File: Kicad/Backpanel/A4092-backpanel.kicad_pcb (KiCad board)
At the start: 2 copper layers, 45 x 90.5 mm, 4 parts, among them J1 Conn_02x25_Odd_Even, J2 5787170-5

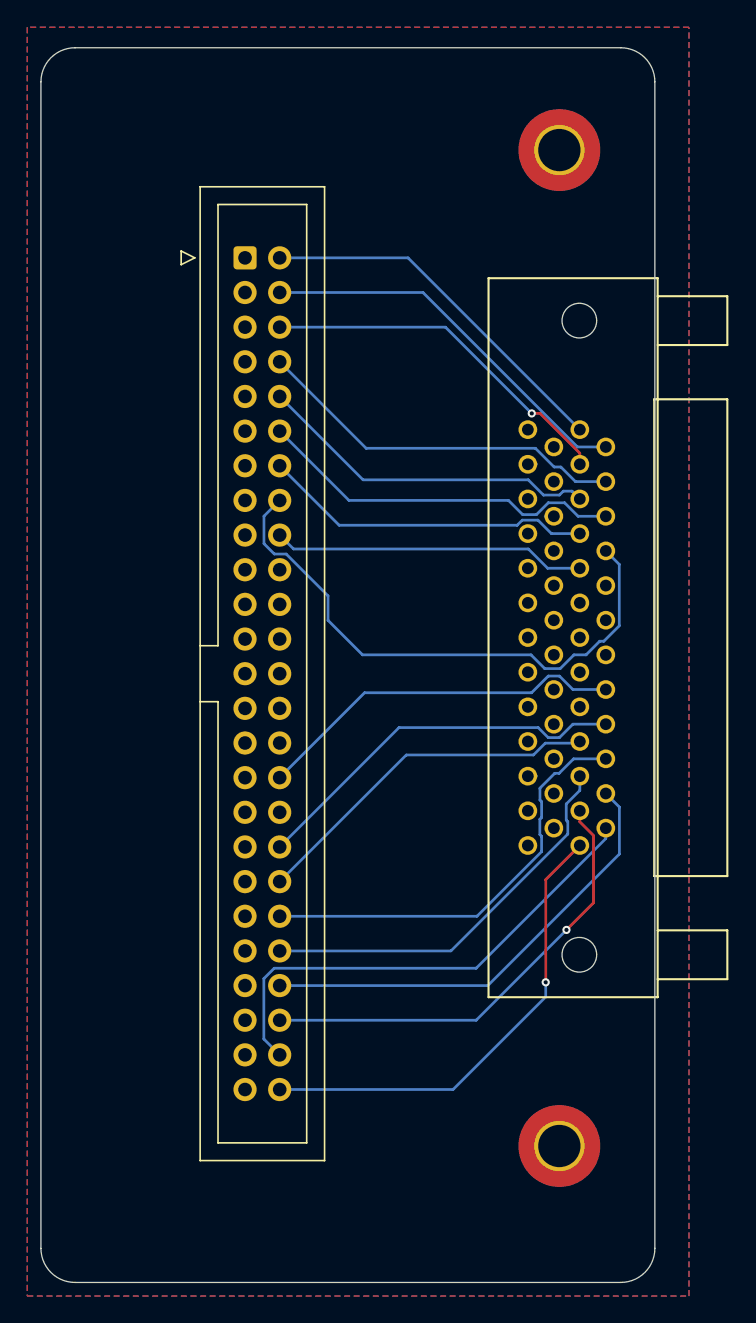
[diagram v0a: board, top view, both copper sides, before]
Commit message: Update Backpanel for smaller footprint
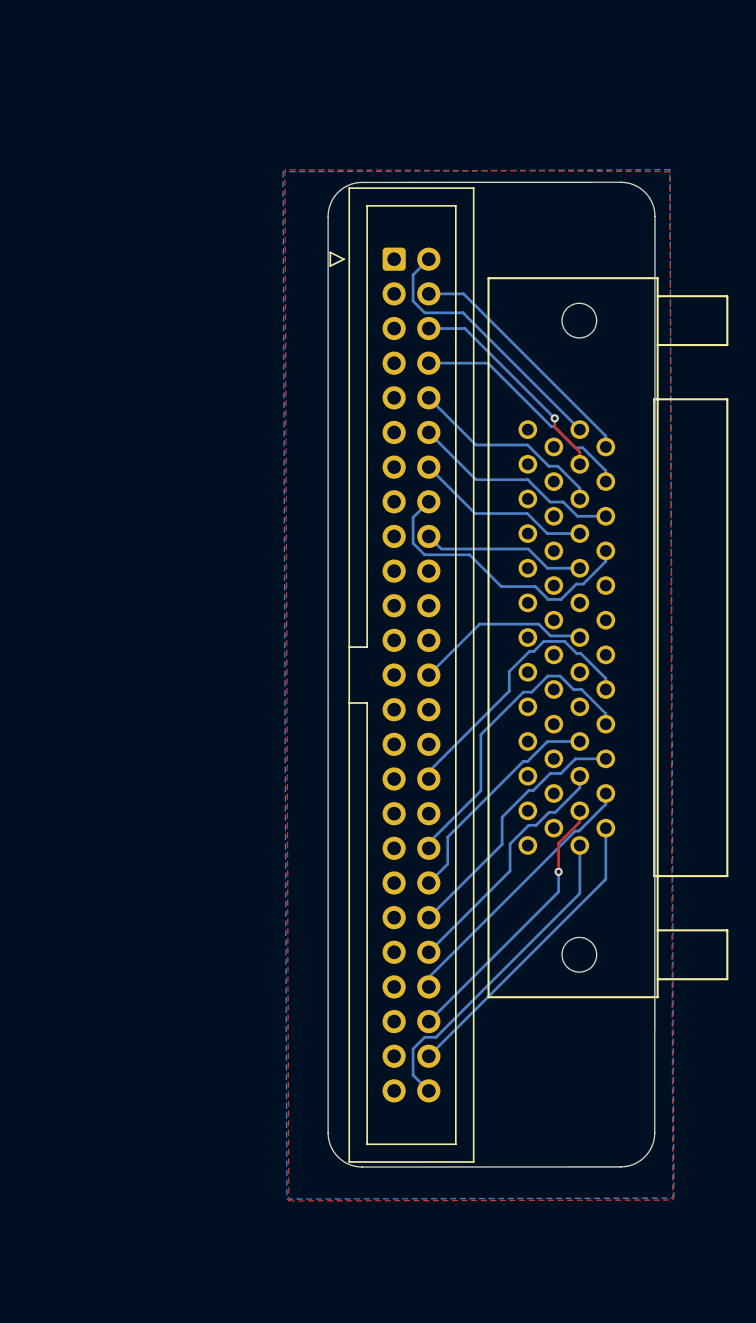
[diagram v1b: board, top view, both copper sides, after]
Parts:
- removed H1, H2: MOUNT_HOLE, StefanHamminga/SH_Mechanical.pretty:MOUNT_HOLE_M3
- moved J1 10.9 mm to (155.9, 65.5)
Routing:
- net SCDAT7: track 41.7 -> 21.3 mm
- net SCTRL_REQ: track 36.2 -> 22.1 mm
- net SCTRL_SEL: track 33.7 -> 19.7 mm
- net SCTRL_CD: track 33.7 -> 20.0 mm
- net SCSI_TERMPWR: track 0.00 -> 13.0 mm
- net SCTRL_RST: track 31.7 -> 19.0 mm
- net SCDAT5: track 27.2 -> 15.5 mm
- net SCTRL_MSG: track 29.4 -> 18.1 mm
- net SCDAT6: track 24.4 -> 13.1 mm
- net SCDATP: track 23.0 -> 12.0 mm
- net SCDAT4: track 25.3 -> 14.6 mm
- net SCDAT2: track 26.6 -> 16.1 mm
- net SCDAT3: track 27.5 -> 17.0 mm
- net SCDAT1: track 28.6 -> 18.1 mm
- net SCTRL_IO: track 34.4 -> 24.0 mm, vias 1 -> 0
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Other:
- board size 45 x 90.5 mm -> 24 x 72.2 mm
